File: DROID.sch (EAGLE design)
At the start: 83 parts

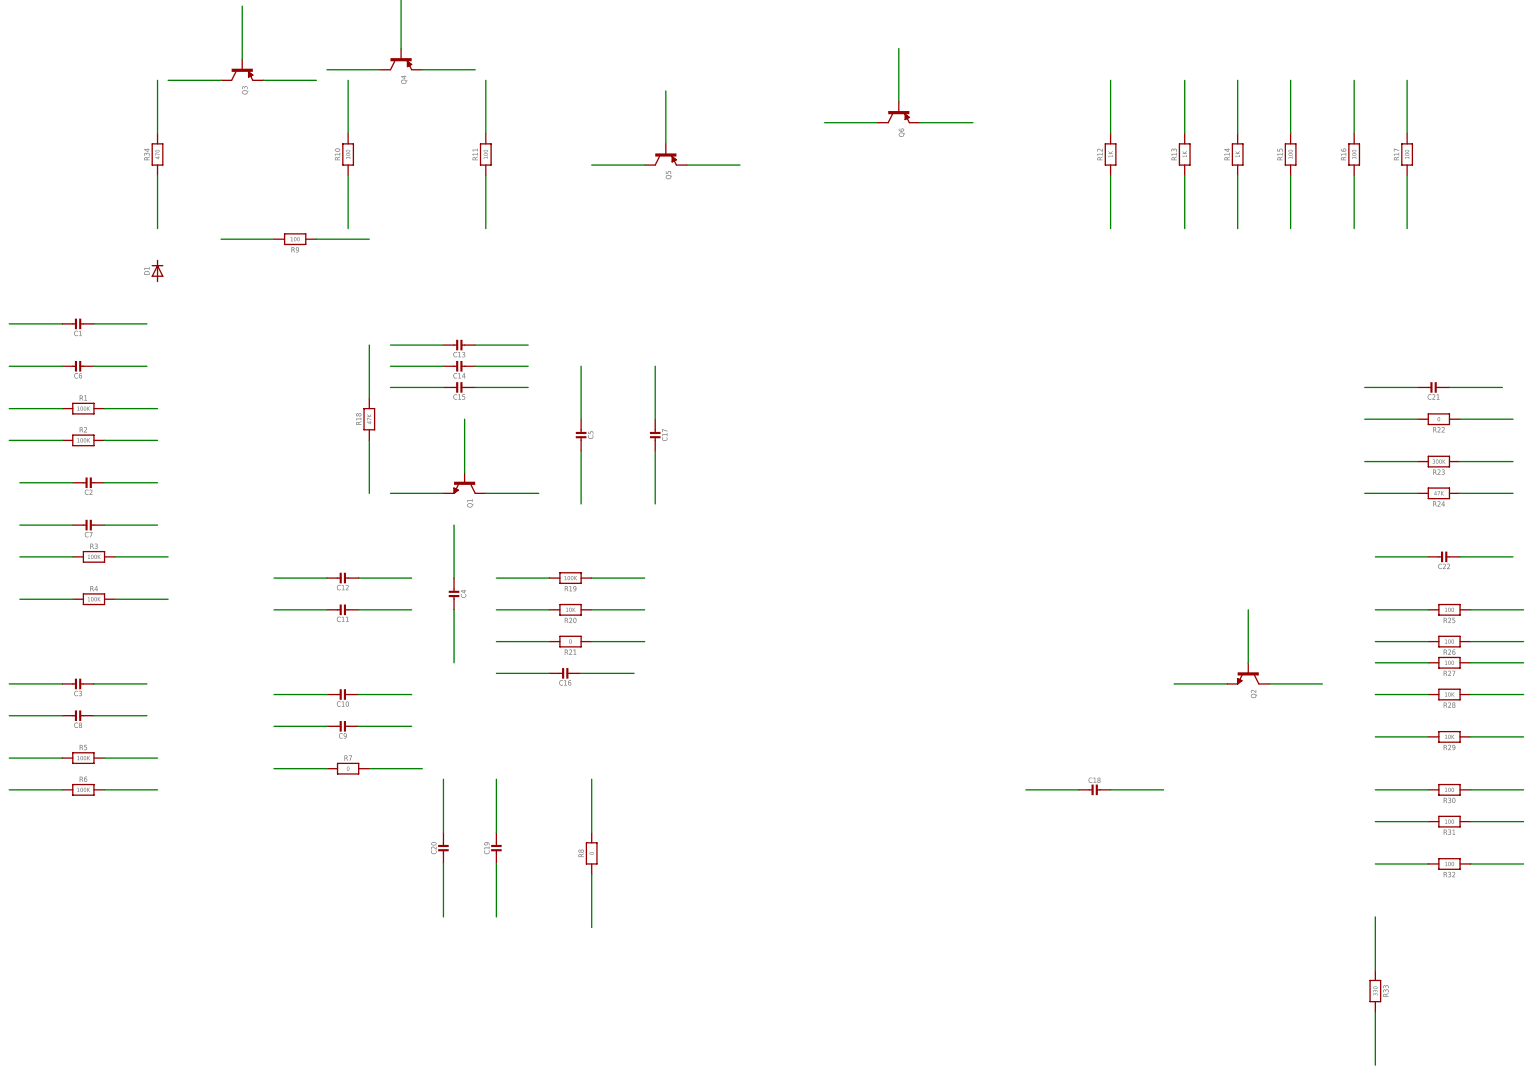
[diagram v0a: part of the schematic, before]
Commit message: fixed passive names
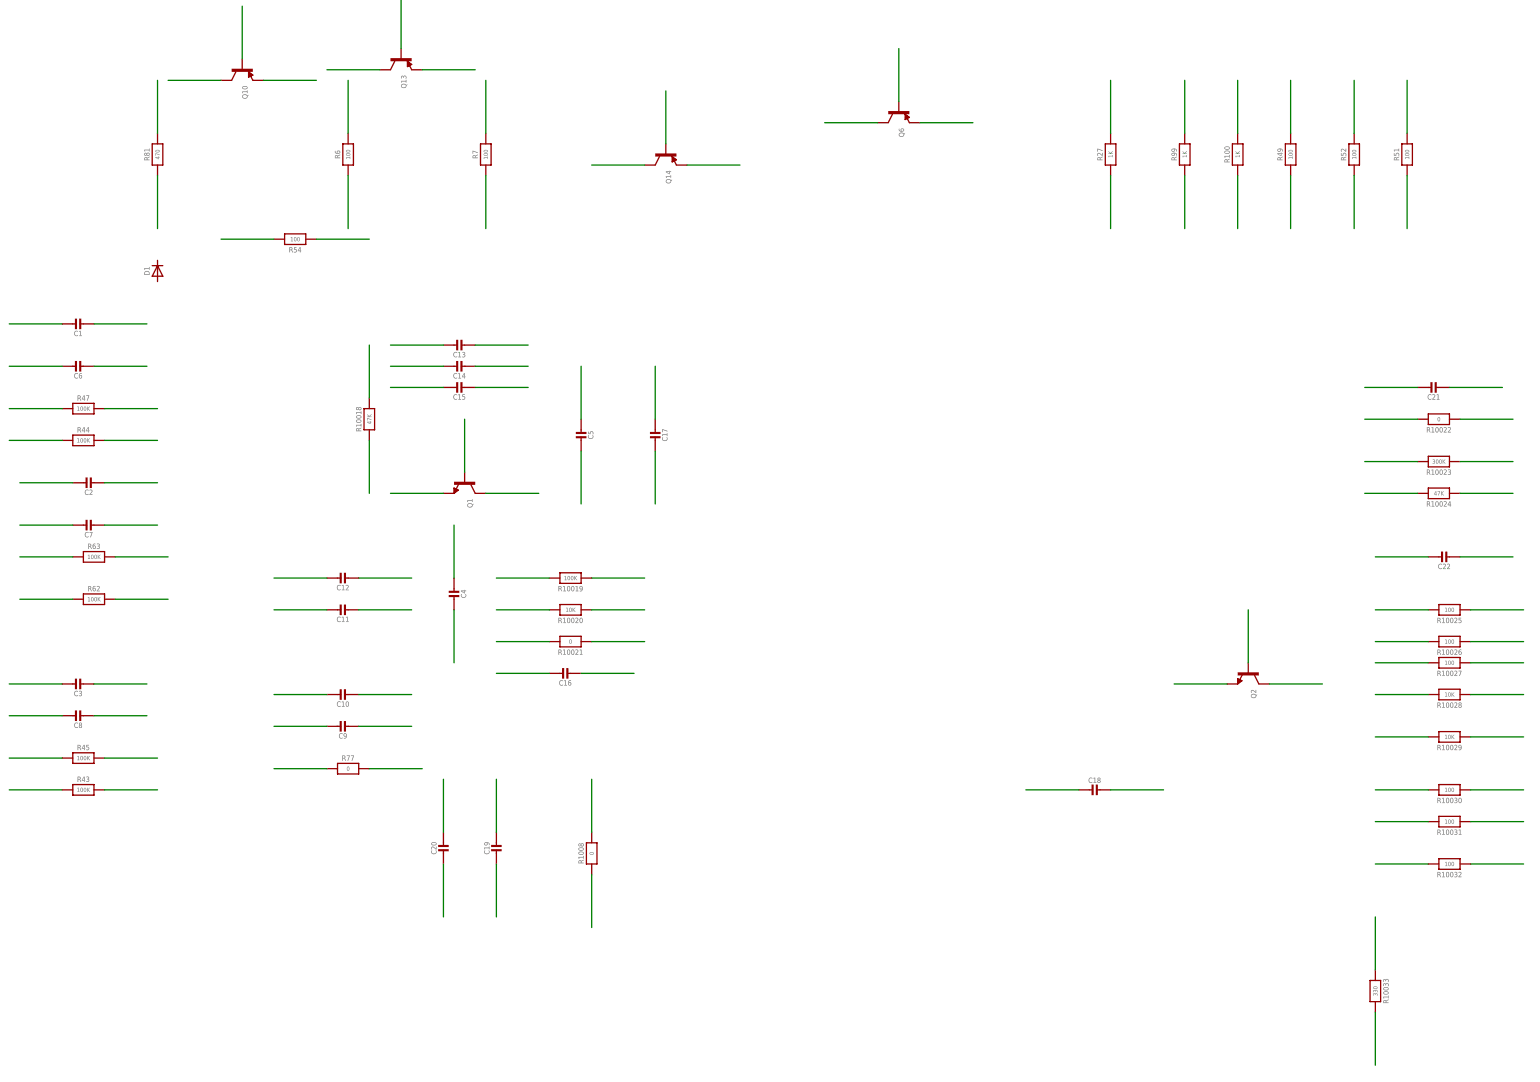
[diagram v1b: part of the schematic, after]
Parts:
- removed R10, R11: 100, microbuilder:RESISTOR_0603_NOOUT
- removed R12: 1K, microbuilder:RESISTOR_0603_NOOUT
- added R10027: 100, microbuilder:RESISTOR_0603_NOOUT
- added R43: 100K, microbuilder:RESISTOR_0603_NOOUT
- added R77: 0, microbuilder:RESISTOR_0603_NOOUT
- R27: value 100 -> 1K
- R6: value 100K -> 100
- R7: value 0 -> 100
- renumbered Q3 to Q10, Q4 to Q13, Q5 to Q14, R1 to R47, R13 to R99, R14 to R100, R15 to R49, R16 to R52, R17 to R51, R18 to R10018, R19 to R10019, R2 to R44, R20 to R10020, R21 to R10021, R22 to R10022, R23 to R10023, R24 to R10024, R25 to R10025, R26 to R10026, R28 to R10028, R29 to R10029, R3 to R63, R30 to R10030, R31 to R10031, R32 to R10032, R33 to R10033, R34 to R81, R4 to R62, R5 to R45, R8 to R1008, R9 to R54
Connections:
- removed net N$32 (its old number): R12.1
- removed net N$33 (its old number): R12.2
- removed net N$34 (its old number): R11.1
- removed net N$35 (its old number): R11.2
- removed net N$36 (its old number): R10.1
- removed net N$37 (its old number): R10.2
- new net N$111: R77.1
- new net N$112: R77.2
- new net N$127: R43.1
- new net N$128: R43.2
- new net N$85: R10027.1
- new net N$86: R10027.2
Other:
- moved on the sheet: R27, R6, R7

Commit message: more renames?
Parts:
- removed C1, C3: (no value), microbuilder:CAP_CERAMIC_0805MP
- removed C12, C6, C8: (no value), microbuilder:CAP_CERAMIC0603_NO
- added C23, C31, C33, C38: (no value), microbuilder:CAP_CERAMIC0603_NO
- C17, C19: device microbuilder:CAP_CERAMIC0603_NO -> microbuilder:CAP_CERAMIC_0805MP
- renumbered C10 to C35, C13 to C25, C14 to C24, C15 to C29, C2 to C28, C20 to C39, C22 to C26, C4 to C20A, C5 to C22A, C7 to C27, C9 to C36, Q1 to Q12, Q2 to Q11, R10018 to R25, R10019 to R71, R10020 to R68, R10021 to R26, R10022 to R76, R10023 to R59, R10024 to R61, R10025 to R55, R10026 to R60, R10027 to R29, R10028 to R23, R10029 to R18, R10030 to R22, R10031 to R66, R10032 to R64, R10033 to R5, R1008 to R30, R47 to R47_OR_42
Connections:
- removed net N$123 (its old number): C8.1
- removed net N$124 (its old number): C8.2
- removed net N$125 (its old number): C3.1
- removed net N$126 (its old number): C3.2
- removed net N$3 (its old number): C6.1
- removed net N$4 (its old number): C6.2
- removed net N$69: C12.1
- removed net N$7 (its old number): C1.1
- removed net N$70: C12.2
- removed net N$8 (its old number): C1.2
- new net N$51: C31.1
- new net N$52: C31.2
- new net N$55: C38.1
- new net N$56: C38.2
- new net N$57: C23.1
- new net N$58: C23.2
- new net N$71: C33.1
- new net N$72: C33.2
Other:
- moved on the sheet: C11, C16, C17, C18, C19, C21

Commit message: renamed nets to make connections easier
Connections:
- net N$1 renamed C27_A
- net N$10 renamed R62_B
- net N$100 renamed R76_B
- net N$101 renamed R68_A
- net N$102 renamed R68_B
- net N$103 renamed R26_A
- net N$104 renamed R26_B
- net N$105 renamed R71_A
- net N$106 renamed R71_B
- net N$107 renamed R25_A
- net N$108 renamed R25_B
- net N$109 renamed R30_A
- net N$11 renamed R44_A
- net N$110 renamed R30_B
- net N$111 renamed R77_A
- net N$112 renamed R77_B
- net N$118 renamed C35_A
- net N$119 renamed C35_B
- net N$12 renamed R44_B
- net N$123 renamed C16_A
- net N$124 renamed C16_B
- net N$125 renamed C17_A
- net N$126 renamed C17_B
- net N$127 renamed R43_A
- net N$128 renamed R43_B
- net N$129 renamed R45_A
- net N$13 renamed R63_A
- net N$130 renamed R45_B
- net N$14 renamed R63_B
- net N$2 renamed C27_B
- net N$20 renamed R81_A
- net N$21 renamed R81_B
- net N$22 renamed R51_A
- net N$23 renamed R51_B
- net N$24 renamed R52_A
- net N$25 renamed R52_B
- net N$26 renamed R49_A
- net N$27 renamed R49_B
- net N$28 renamed R100_A
- net N$29 renamed R100_B
- net N$3 renamed C18_A
- net N$30 renamed R99_A
- net N$31 renamed R99_B
- net N$32 renamed R27_A
- net N$33 renamed R27_B
- net N$34 renamed R7_A
- net N$35 renamed R7_B
- net N$36 renamed R6_A
- net N$37 renamed R6_B
- net N$38 renamed R54_A
- net N$39 renamed R54_B
- net N$4 renamed C18_B
- net N$49 renamed C26_A
- net N$5 renamed C28_A
- net N$50 renamed C26_B
- net N$51 renamed C31_A
- net N$52 renamed C31_B
- net N$53 renamed C39_A
- net N$54 renamed C39_B
- net N$55 renamed C38_A
- net N$56 renamed C38_B
- net N$57 renamed C23_A
- net N$58 renamed C23_B
- net N$59 renamed C21_A
- net N$6 renamed C28_B
- net N$60 renamed C21_B
- net N$61 renamed C29_A
- net N$62 renamed C29_B
- net N$63 renamed C24_A
- net N$64 renamed C24_B
- net N$65 renamed C11_A
- net N$66 renamed C11_B
- net N$67 renamed C25_A
- net N$68 renamed C25_B
- net N$7 renamed C19_A
- net N$71 renamed C33_A
- net N$72 renamed C33_B
- net N$73 renamed R5_A
- net N$74 renamed R5_B
- net N$75 renamed R64_A
- net N$76 renamed R64_B
- net N$77 renamed C36_A
- net N$78 renamed C36_B
- net N$79 renamed R66_A
- net N$8 renamed C19_B
- net N$80 renamed R66_B
- net N$81 renamed R18_A
- net N$82 renamed R18_B
- net N$83 renamed R23_A
- net N$84 renamed R23_B
- net N$85 renamed R29_A
- net N$86 renamed R29_B
- net N$87 renamed R60_A
- net N$88 renamed R60_B
- net N$89 renamed R22_A
- net N$9 renamed R62_A
- net N$90 renamed R22_B
- net N$91 renamed R55_A
- net N$92 renamed R55_B
- net N$95 renamed R61_A
- net N$96 renamed R61_B
- net N$97 renamed R59_A
- net N$98 renamed R59_B
- net N$99 renamed R76_A

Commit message: net name/connection updates
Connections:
- net LED- renamed PAIR_LED-
- net N$115 renamed Q11_B
- net N$116 renamed Q11_E
- net N$117 renamed Q11_C
- net N$120 renamed Q12_B
- net N$121 renamed Q12_E
- net N$131 renamed HEAD_OUT_B
- net N$132 renamed HEAD_OUT_A
- net N$139 renamed RIGHT_OUT_B
- net N$140 renamed RIGHT_OUT_A
- net N$141 renamed RIGHT_IN_B
- net N$142 renamed RIGHT_IN_A
- net N$147 renamed LEFT_OUT_B
- net N$148 renamed LEFT_OUT_A
- net N$17 renamed Q14_B
- net N$18 renamed Q14_C
- net N$19 renamed Q14_E
- net N$40 renamed Q6_B
- net N$41 renamed Q6_C
- net N$42 renamed Q6_E
- net N$43 renamed Q13_B
- net N$44 renamed Q13_C
- net N$45 renamed Q13_E
- net N$46 renamed Q10_B
- net N$47 renamed Q10_C
- net N$48 renamed Q10_E
- removed net LED+: JP11.3
- removed net N$122: Q12.C
- removed net N$133: U$3.IN_B
- removed net N$134: U$3.IN_A
- removed net N$149: U$1.IN_B
- removed net N$150: U$1.IN_A
- removed net P0.00: U$4.P0.00
- removed net P0.1: U$4.P0.1
- removed net P0.10: U$4.P0.10
- removed net P0.11: U$4.P0.11
- removed net P0.12: U$4.P0.12
- removed net P0.13: U$4.P0.13
- removed net P0.16: U$4.P0.16
- removed net P0.2: U$4.P0.2
- removed net P0.20: U$4.P0.20
- removed net P0.21: U$4.P0.21
- removed net P0.22: U$4.P0.22
- removed net P0.23: U$4.P0.23
- removed net P0.24: U$4.P0.24
- removed net P0.25: U$4.P0.25
- removed net P0.26: U$4.P0.26
- removed net P0.27: U$4.P0.27
- removed net P0.28: U$4.P0.28
- removed net P0.29: U$4.P0.29
- removed net P0.3: U$4.P0.3
- removed net P0.30: U$4.P0.30
- removed net P0.4: U$4.P0.4
- removed net P0.5: U$4.P0.5
- removed net P0.6: U$4.P0.6
- removed net P0.7: U$4.P0.7
- removed net P0.8: U$4.P0.8
- removed net P0.9: U$4.P0.9
- removed net PAIR: JP11.1
- removed net Q12_COL: U$5.5
- removed net R100: U$5.15
- removed net R25: U$5.6
- removed net R27: U$5.9
- removed net R99: U$5.14
- new net HEAD_IN_A: U$3.IN_A, U$4.P0.23
- new net HEAD_IN_B: U$3.IN_B, U$4.P0.24
- new net LEFT_IN_A: U$1.IN_A, U$4.P0.25
- new net LEFT_IN_B: U$1.IN_B, U$4.P0.30
- new net PAIR_BTN: JP11.1, U$4.P0.13
- new net PAIR_LED+: JP11.3, U$4.P0.11
- new net Q12_C: Q12.C, U$5.5
- net GND: now also U$4.P0.29
- net R100_B: now also U$5.15
- net R22_B: now also U$4.P0.1
- net R23_B: now also U$4.P0.5
- net R25_B: now also U$5.6
- net R27_B: now also U$5.9
- net R29_B: now also U$4.P0.4
- net R49_B: now also U$4.P0.2
- net R51_B: now also U$4.P0.22
- net R52_B: now also U$4.P0.7
- net R55_B: now also U$4.P0.3
- net R62_B: now also U$4.P0.8
- net R63_B: now also U$4.P0.9
- net R64_B: now also U$4.P0.12
- net R99_B: now also U$5.14
- net SWCLK: now also U$4.P0.16
- net SWDIO: now also U$4.P0.20
- net VCC_3: now also U$4.P0.00
- net VCC_33: now also U$4.P0.28
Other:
- note added: "Connections to passives have the _B net towards the nrf or mystery module"
- note added: "HEAD"
- note added: "LEFT"
- note added: "RIGHT"

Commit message: more nets/conns, addition parts
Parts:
- removed D1: (no value), microbuilder:DIODESOD-323
- added C34: (no value), microbuilder:CAP_CERAMIC0603_NO
- added C37: 100uF, microbuilder:CAP_ELECTROLYTICPANASONIC_D
- added D14: (no value), microbuilder:DIODESOD-323
- added F1: (no value), microbuilder:PTC1812
- added L11, L12: (no value), microbuilder:INDUCTOR0603_NO
- added L13, L14, L9: (no value), microbuilder:INDUCTOR0805-NO
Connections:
- removed net C11_A: C11.1
- removed net C16_A: C16.1
- removed net C17_A: C17.1
- removed net C18_A: C18.1
- removed net C19_A: C19.1
- removed net C21_A: C21.1
- removed net C26_A: C26.1
- removed net C26_B: C26.2
- removed net C27_A: C27.1
- removed net C28_A: C28.1
- removed net C31_A: C31.1
- removed net C31_B: C31.2
- removed net C33_A: C33.1
- removed net C35_A: C35.1
- removed net C36_A: C36.1
- removed net C38_A: C38.1
- removed net HE_M_A: JP5.1
- removed net HE_M_B: JP5.2
- removed net LM_A: JP3.1
- removed net LM_B: JP3.2
- removed net N$136: U$3.GND
- removed net N$144: U$2.GND
- removed net N$15: R47_OR_42.1
- removed net N$152: U$1.GND
- removed net N$93: C20A.1
- removed net Q11_E: Q11.E
- removed net Q12_E: Q12.E
- removed net R18_A: R18.1
- removed net R18_B: R18.2
- removed net R23_A: R23.1
- removed net R43_A: R43.1
- removed net R44_A: R44.1
- removed net R45_A: R45.1
- removed net R55_A: R55.1
- removed net R59_A: R59.1
- removed net R5_A: R5.1
- removed net R5_B: R5.2
- removed net R60_A: R60.1
- removed net R60_B: R60.2
- removed net R61_B: R61.2
- removed net R62_A: R62.1
- removed net R63_A: R63.1
- removed net R66_A: R66.1
- removed net R66_B: R66.2
- removed net R71_A: R71.1
- removed net R81_A: R81.1
- removed net R81_B: R81.2
- removed net RM_A: JP4.1
- removed net RM_B: JP4.2
- new net C34_B: C34.2
- new net D14_A: D14.A
- new net F1_1: F1.1
- new net F1_2: F1.2
- new net L11_1: L11.1
- new net L11_2: L11.2
- new net L12_1: L12.1
- new net L12_2: L12.2
- new net L13_1: L13.1
- new net L13_2: L13.2
- new net L14_1: L14.1
- new net L14_2: L14.2
- new net L9_1: L9.1
- new net L9_2: L9.2
- net GND: now also C11.1, C16.1, C17.1, C18.1, C19.1, C20A.1, C21.1, C26.2, C27.1, C28.1, C31.1, C33.1, C34.1, C35.1, C36.1, C37.-, C38.1, Q11.E, Q12.E, R43.1, R44.1, R45.1, R47_OR_42.1, R5.1, R61.2, R62.1, R63.1, R66.1, R71.1, R81.1, U$1.GND, U$2.GND, U$3.GND
- net HEAD_OUT_B: now also JP5.1, JP5.2
- net LEFT_OUT_A: now also JP3.1
- net LEFT_OUT_B: now also JP3.2
- net OFF: now also R81.2
- net PAIR_LED-: now also R5.2
- net Q10_B: now also R60.2
- net Q11_C: now also R60.1
- net R22_A: now also R18.1
- net R23_B: now also R18.2
- net R29_A: now also R23.1
- net R61_A: now also C26.1, R55.1, R59.1
- net R64_B: now also R66.2
- net R76_B: now also C31.2
- net RIGHT_OUT_A: now also JP4.1
- net RIGHT_OUT_B: now also JP4.2
- net VCC_ON: now also C37.+, D14.C
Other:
- note added: "should be 2920"
- moved on the sheet: C11, C16, C17, C18, C19, C20A, C21, C22A, C23, C24, C25, C26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

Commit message: all components?
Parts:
- added U7, U8: (no value), microbuilder:ME62XX
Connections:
- removed net C11_B: C11.2
- removed net C33_B: C33.2
- removed net C34_B: C34.2
- removed net C35_B: C35.2
- removed net C36_B: C36.2
- removed net L9_1: L9.1
- removed net L9_2: L9.2
- removed net Q10_E: Q10.E
- removed net R100_A: R100.1
- removed net R25_A: R25.1
- removed net R59_B: R59.2
- removed net R64_A: R64.1
- removed net R76_B: C31.2, R76.2
- removed net R77_B: R77.2
- removed net R99_A: R99.1
- new net U7_VIN: C34.2, U7.VSS
- new net U7_VOUT: C33.2, L9.2, Q10.E, U7.VOUT
- new net U8_VIN: C35.2, L9.1, U8.VSS
- new net U8_VOUT: C36.2, R25.1, R77.2, U8.VOUT
- net GND: now also U7.VIN, U8.VIN
- net Q10_C: now also R59.2
- net Q11_B: now also R64.1
- net Q13_B: now also R99.1
- net Q14_B: now also R100.1
- net R76_A: now also C11.2
- net VCC_33: now also C31.2, R76.2
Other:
- moved on the sheet: C20A, C21, C22A, C23, C24, C25, C29, L9, Q10, Q11, Q12, R100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

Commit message: getti'n close
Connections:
- removed net Q13_E: Q13.E
- removed net Q14_E: Q14.E
- removed net Q6_C: Q6.C
- removed net Q6_E: Q6.E
- removed net R22_A: R18.1, R22.1
- removed net R27_A: R27.1
- removed net R29_A: R23.1, R29.1
- removed net R49_A: R49.1
- removed net R51_A: R51.1
- removed net R52_A: R52.1
- removed net R68_A: R68.1
- removed net R68_B: R68.2
- removed net R6_A: R6.1
- removed net R6_B: R6.2
- removed net R71_B: R71.2
- removed net R7_A: R7.1
- removed net R7_B: R7.2
- removed net VCC_5V: JP14.5, U$5.2, U$5.23, U$5.32, U$5.4, U$5.7
- net HE_5V: now also Q6.C
- net H_L: now also R52.1
- net H_MID: now also R49.1
- net H_R: now also R51.1
- net L_ID: now also R18.1, R22.1
- net L_LED: now also R6.1
- net P0.14: now also R68.2, R71.2; no longer U$5.18
- net P0.15: now also U$5.18; no longer U$5.19
- net Q12_B: now also R68.1
- net Q13_C: now also R6.2
- net Q14_C: now also R7.1
- net Q6_B: now also R27.1
- net R_ID: now also R23.1, R29.1
- net R_LED: now also R7.2
- net SWCLK: now also U$5.19
- net U7_VOUT: now also Q13.E, Q14.E, Q6.E
- net VCC_33: now also JP14.5, U$5.2, U$5.23, U$5.32, U$5.4, U$5.7
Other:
- note added: "NC"
- note added: "Why is this all the way over here?!"
- moved on the sheet: C20A, JP1, JP10, JP13, JP7, JP8, R6, R68, R7

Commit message: done for now
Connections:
- removed net C19_B: C19.2
- removed net C21_B: C21.2
- removed net C23_A: C23.1
- removed net C23_B: C23.2
- removed net C24_A: C24.1
- removed net C24_B: C24.2
- removed net C25_A: C25.1
- removed net C25_B: C25.2
- removed net C29_A: C29.1
- removed net C29_B: C29.2
- removed net C38_B: C38.2
- removed net C39_A: C39.1
- removed net C39_B: C39.2
- removed net F1_1: F1.1
- removed net F1_2: F1.2
- removed net L11_1: L11.1
- removed net L11_2: L11.2
- removed net L12_1: L12.1
- removed net L12_2: L12.2
- removed net L13_1: L13.1
- removed net L13_2: L13.2
- removed net L14_1: L14.1
- removed net L14_2: L14.2
- removed net N$113: C22A.1
- removed net N$114: C22A.2
- removed net N$94: C20A.2
- removed net R26_B: R26.2
- removed net R30_A: R30.1
- removed net R30_B: R30.2
- removed net R54_A: R54.1
- removed net R54_B: R54.2
- removed net R77_A: R77.1
- removed net U7_VOUT: C33.2, L9.2, Q10.E, Q13.E, Q14.E, Q6.E, U7.VOUT
- new net GND_INDUCTED: L14.2, U7.VIN
- new net SP+_OUT: C38.2, JP6.1, L12.1
- new net SP-_OUT: C39.2, JP6.2, L11.1
- net BAT+: now also F1.2
- net GND: now also C22A.1, C23.1, C24.1, C25.1, C29.1, C39.1, L14.1; no longer U7.VIN
- net Q10_B: now also R54.2
- net Q12_C: now also C29.2
- net R26_A: now also C21.2
- net SP+: now also L12.2; no longer JP6.1
- net SP-: now also L11.2; no longer JP6.2
- net U7_VIN: now also L13.2, Q10.E, R54.1
- net U8_VOUT: now also C24.2, C25.2, R77.1
- net VCC_33: now also C20A.2, C22A.2, C23.2, C33.2, L9.2, Q13.E, Q14.E, Q6.E, R26.2, R30.1, R30.2, U7.VOUT
- net VCC_ON: now also L13.1
- net VCV_M: now also C19.2, F1.1
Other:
- note added: "Why is C11 all the way over here?!"
- note removed: "Why is this all the way over here?!"
- moved on the sheet: C11, C21, C24, C25, C29, C37, C38, C39, D14, F1, JP14, JP15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
